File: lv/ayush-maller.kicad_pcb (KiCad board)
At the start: 2 copper layers, 196 x 16 mm, 2 parts

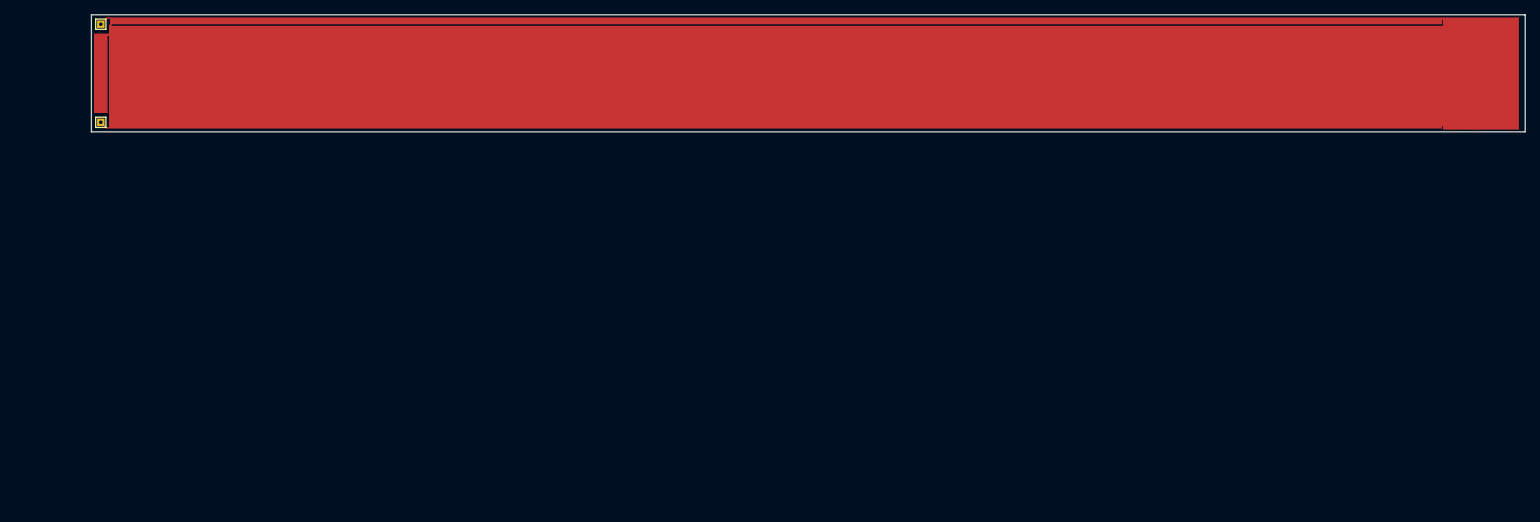
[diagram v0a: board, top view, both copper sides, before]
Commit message: Assign footprints and update PCB from schematic
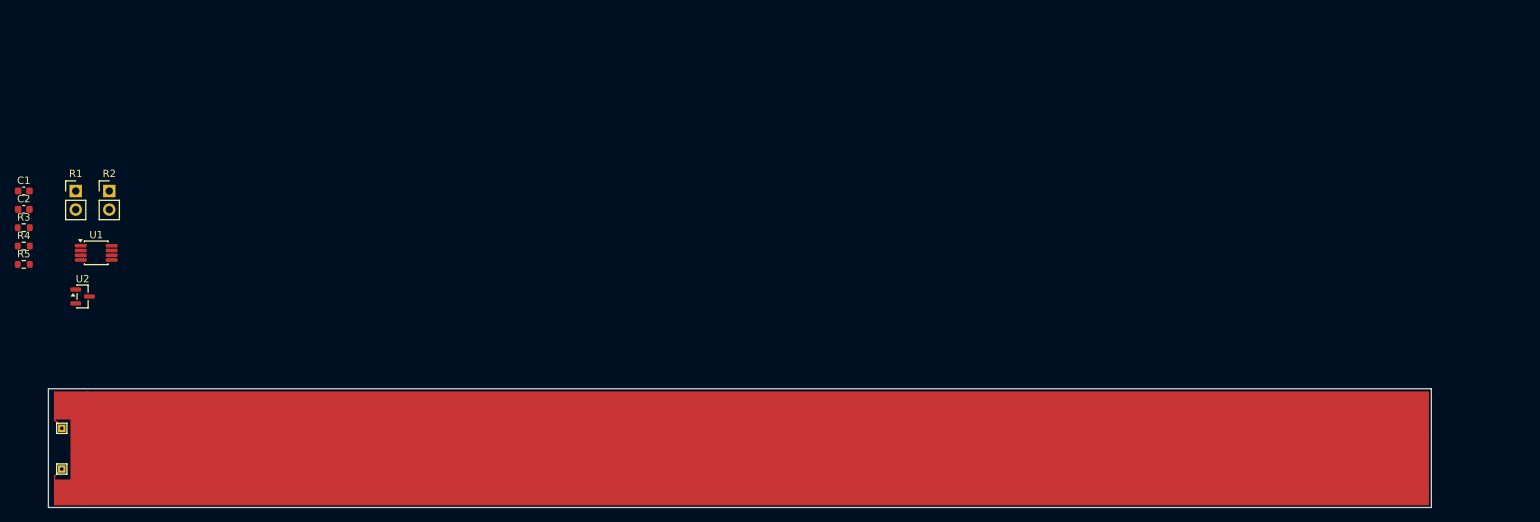
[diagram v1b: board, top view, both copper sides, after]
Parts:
- removed the REF** at (51.3, 51.3)
- removed the REF** at (51.3, 64.7)
- added C1: 100n, Capacitor_SMD:C_0603_1608Metric, F.Cu at (40.8, 74.1)
- added C2: 100n, Capacitor_SMD:C_0603_1608Metric, F.Cu at (40.8, 76.6)
- added R1: GAUGE, Connector_PinHeader_2.54mm:PinHeader_1x02_P2.54mm_Vertical, F.Cu at (47.9, 74.1)
- added R2: GAUGE_90, Connector_PinHeader_2.54mm:PinHeader_1x02_P2.54mm_Vertical, F.Cu at (52.4, 74.1)
- added R3: 350, Resistor_SMD:R_0603_1608Metric, F.Cu at (40.8, 79.1)
- added R4: 350, Resistor_SMD:R_0603_1608Metric, F.Cu at (40.8, 81.6)
- added R5: 2.49k, Resistor_SMD:R_0603_1608Metric, F.Cu at (40.8, 84.1)
- added REF**: TestPoint_THTPad_1.0x1.0mm_Drill0.5mm, TestPoint:TestPoint_THTPad_1.0x1.0mm_Drill0.5mm, F.Cu at (45.9, 106.5)
- added REF**: TestPoint_THTPad_1.0x1.0mm_Drill0.5mm, TestPoint:TestPoint_THTPad_1.0x1.0mm_Drill0.5mm, F.Cu at (45.9, 112.1)
- added U1: INA333xxDGK, Package_SO:VSSOP-8_3x3mm_P0.65mm, F.Cu at (50.7, 82.5)
- added U2: REF3012, Package_TO_SOT_SMD:SOT-23, F.Cu at (48.8, 88.5)
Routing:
- net sg: track 19041.3 -> 19046.8 mm
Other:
- board size 196 x 16 mm -> 189.1 x 16.2 mm
